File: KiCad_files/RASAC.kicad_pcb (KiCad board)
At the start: 6 copper layers, 147 x 85 mm, 386 parts, among them J1 PCIe_x4_Connector, J10 AS4C128M16D2A, J11 AS4C128M16D2A, J12 Conn_01x03, J13 Conn_02x03_Counter_Clockwise, J14 Conn_01x02, J2 PCIe_6_Pin_Power, J3 Conn_01x06, J4 USB_C_Receptacle, J5 TFP410, J6 DB15_Female_HighDensity_Mount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, J7 HDMI_A_1.4, J8 Conn_01x02, J9 Conn_01x02, Q1 Q_NMOS_GSD, Q2 Q_PMOS_GSD, SW1 SW_Push, U1 XC7A35T_CSG325, U10 W25Q128JV, U11 TPD12S521, U12 PCA9306, U13 LM2676-KTW, U2 MAX15027, U3 PI3420, U4 PI3421, U5 PI3420, U6 FT2232HL, U7 93LCxxC, U8 SiT8209, U9 SiT9102, Y1 12MHz

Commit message: PCB Layout
Don't remember what changed, but gonna push before my computer dies again
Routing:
- net VCC1V8: track 44.7 -> 146.7 mm, vias 0 -> 23
- net GND: vias 70 -> 115

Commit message: Initial FPGA routing + 3D RAM
Slowly losing insanity while listening to WII music for hours
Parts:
- J10, J11: footprint Housings_BGA:BGA-90_2x3x15_8.0x13.0mm_Pitch0.8mm -> custom:BGA-90_2x3x15_8.0x13.0mm_Pitch0.8mm
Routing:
- net VCC1V8: track 146.7 -> 213.3 mm, vias 23 -> 35
- net MGTAVCC: track 97.8 -> 125.2 mm, vias 2 -> 3
- net PCIe_RX2_P: track 29.4 -> 3.03 mm, vias 2 -> 1
- net PCIe_RX2_N: track 28.7 -> 2.92 mm, vias 2 -> 1
- net PCIe_RX1_P: track 26.7 -> 1.25 mm, vias 2 -> 0
- net GND: track 850.9 -> 875.9 mm, vias 115 -> 139
- net PCIe_RX3_N: track 28.1 -> 3.16 mm, vias 2 -> 1
- net PCIe_RX1_N: track 26.1 -> 1.19 mm, vias 2 -> 0
- net PCIe_RX3_P: track 28.8 -> 4.08 mm, vias 2 -> 1
- net PCIe_TX3_N: track 25.8 -> 1.27 mm, vias 2 -> 0
- net PCIe_TX3_P: track 26.4 -> 2.17 mm, vias 2 -> 0
- net PCIe_TX2_N: track 20.9 -> 1.26 mm, vias 2 -> 0
- net PCIe_TX2_P: track 21.5 -> 2.22 mm, vias 2 -> 0
- net PCIe_RX0_N: track 22.5 -> 3.16 mm, vias 2 -> 1
- net PCIe_RX0_P: track 23.1 -> 4.08 mm, vias 2 -> 1
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
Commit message: PCIe + RAM Layout?
Is this PCIe even going to work...?
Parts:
- U1: moved to B.Cu
- moved J13 29.0 mm to (105.6, 118.2)
- moved U10 17.3 mm to (116.3, 127.9)
- moved R1 9.12 mm to (117.5, 113.3)
- moved U8 9.12 mm to (113.8, 109.7)
- moved J14 9.12 mm to (116.2, 101.2)
- moved J9 9.12 mm to (123.1, 101.1)
- moved SW1 9.12 mm to (125.5, 110.5)
- moved U12 6.56 mm to (135.7, 106.6)
- moved J11 6.29 mm to (168.9, 114.3), turned to 270 degrees
- moved J10 5.24 mm to (168.9, 125.9), turned to 270 degrees
- moved U1 4.31 mm to (149.1, 126.3)
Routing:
- net VCC1V8: track 213.3 -> 93.9 mm, vias 35 -> 57
- net DDR2_DQSU_C: track 2.35 -> 46.3 mm, vias 0 -> 3
- net DDR2_DQSU_T: track 4.96 -> 36.7 mm, vias 1 -> 3
- net DDR2_DMU: track 2.36 -> 32.2 mm, vias 0 -> 1
- net PCIe_RX1_P: track 1.25 -> 29.0 mm, vias 0 -> 1
- net PCIe_RX1_N: track 1.19 -> 28.5 mm, vias 0 -> 1
- net DDR2_DQSL_T: track 4.16 -> 29.7 mm, vias 1 -> 3
- net DDR2_DQSL_C: track 4.97 -> 29.6 mm, vias 1 -> 4
- net DDR2_DML: track 1.41 -> 24.8 mm, vias 0 -> 3
- net PCIe_RX2_N: track 2.92 -> 26.0 mm, vias 1 -> 2
- net PCIe_RX2_P: track 3.03 -> 25.9 mm, vias 1 -> 2
- net PCIe_RX0_P: track 4.08 -> 25.6 mm
- net PCIe_RX0_N: track 3.16 -> 24.7 mm
- net DDR2_CK_T: track 1.40 -> 20.7 mm, vias 0 -> 2
- net DDR2_CK_C: track 4.93 -> 23.7 mm, vias 1 -> 3
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
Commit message: RAM+FPGA Attempt #1
Oh geez
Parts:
- J10: moved to B.Cu
- moved J10 45.2 mm to (124.2, 132.4)
- moved Q2 31.5 mm to (99.9, 150.9)
- moved Q1 31.5 mm to (101.4, 155.1)
- moved U10 23.5 mm to (100.4, 145.3)
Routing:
- net DDR2_DQ4: track 14.3 -> 40.8 mm, vias 1 -> 2
- net DDR2_DQ9: track 19.3 -> 41.2 mm, vias 2 -> 3
- net DDR2_DQ10: track 19.2 -> 38.8 mm, vias 3 -> 5
- net DDR2_DQ14: track 16.5 -> 35.0 mm, vias 1 -> 2
- net DDR2_DQ8: track 18.1 -> 36.3 mm, vias 1 -> 2
- net DDR2_DQ15: track 21.2 -> 39.1 mm, vias 2 -> 4
- net DDR2_DQ2: track 19.2 -> 36.8 mm, vias 3 -> 4
- net DDR2_DQ5: track 13.7 -> 30.9 mm
- net DDR2_A6: track 14.1 -> 29.1 mm, vias 1 -> 2
- net DDR2_DQ1: track 18.0 -> 32.7 mm, vias 2 -> 3
- net DDR2_A13: track 11.2 -> 25.7 mm
- net DDR2_A11: track 11.9 -> 25.6 mm, vias 1 -> 2
- net DDR2_A8: track 12.9 -> 26.3 mm
- net DDR2_DQ12: track 18.3 -> 31.2 mm, vias 2 -> 3
- net DDR2_DQ11: track 19.9 -> 32.8 mm, vias 3 -> 4
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
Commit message: RAM+FPGA Attempt #2
Plus some power connections
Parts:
- J11: moved to B.Cu
- moved J11 10.7 mm to (169.7, 124.9)
- moved J10 2.94 mm to (126.8, 131.2)
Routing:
- net GND: track 866.5 -> 944.3 mm, vias 171 -> 180
- net VCC1V8: track 93.9 -> 163.4 mm, vias 57 -> 59
- net DDR2_DQ6: track 13.2 -> 38.4 mm, vias 1 -> 2
- net DDR2_DQ3: track 17.1 -> 40.7 mm, vias 3 -> 4
- net DDR2_DQ0: track 18.2 -> 35.8 mm
- net DDR2_DQ7: track 15.4 -> 31.8 mm
- net DDR2_DQSU_T: track 36.7 -> 22.3 mm, vias 3 -> 2
- net DDR2_DQSU_C: track 34.9 -> 21.2 mm, vias 3 -> 2
- net DDR2_DMU: track 32.2 -> 19.2 mm
- net DDR2_DQ13: track 16.4 -> 28.9 mm, vias 1 -> 2
- net DDR2_DQSL_T: track 29.7 -> 18.5 mm, vias 3 -> 2
- net DDR2_DQ1: track 32.7 -> 43.5 mm
- net DDR2_DQSL_C: track 29.6 -> 19.3 mm, vias 4 -> 3
- net DDR2_DML: track 24.8 -> 15.0 mm, vias 3 -> 2
- net DDR2_DQ10: track 38.8 -> 29.1 mm, vias 5 -> 3
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- added copper zone on Power, net VCC1V8

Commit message: OH MY GOD
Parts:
- R1: moved to B.Cu
- moved C11 178.0 mm to (222.0, 121.6)
- moved TP6 157.3 mm to (220.6, 93.1)
- moved R5 73.6 mm to (114.6, 136.0), turned to 90 degrees
- moved TP16 64.9 mm to (112.4, 134.4)
- moved TP15 64.2 mm to (114.3, 133.4)
- moved R1 45.5 mm to (160.0, 129.7)
- moved J11 43.2 mm to (126.8, 119.6)
- moved Q1 29.1 mm to (117.1, 130.6), turned to 180 degrees
- moved Q2 22.2 mm to (117.1, 136.7)
- moved C211 21.3 mm to (65.9, 106.4)
- moved SW1 19.5 mm to (121.3, 91.5)
- moved U8 10.5 mm to (106.6, 102.1)
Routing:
- net PCIe_12V: track 226.6 -> 299.8 mm, vias 5 -> 46
- net PCIe_3.3V: track 0.00 -> 51.9 mm, vias 0 -> 4
- net PCIe_CLK_P: track 5.55 -> 34.0 mm, vias 1 -> 3
- net PCIe_CLK_N: track 5.15 -> 33.5 mm, vias 1 -> 3
- net MGTAVTT: track 65.1 -> 92.9 mm, vias 1 -> 3
- net DDR2_A0: track 24.4 -> 44.2 mm, vias 1 -> 2
- net DDR2_DQ24: track 15.9 -> 35.6 mm
- net DDR2_DQSU_T: track 22.3 -> 4.96 mm, vias 2 -> 1
- net DDR2_CK_T: track 12.6 -> 27.9 mm, vias 1 -> 2
- net DDR2_DQSU_C: track 21.2 -> 6.20 mm, vias 2 -> 0
- net GND: track 944.3 -> 929.5 mm, vias 180 -> 157
- net DDR2_DMU: track 19.2 -> 5.57 mm, vias 1 -> 0
- net DDR2_DQ31: track 14.8 -> 1.35 mm, vias 1 -> 0
- net DDR2_A2: track 20.4 -> 33.4 mm, vias 3 -> 4
- net DDR2_DQ30: track 14.3 -> 1.35 mm, vias 1 -> 0
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- added copper zone on Power, net PCIe_12V

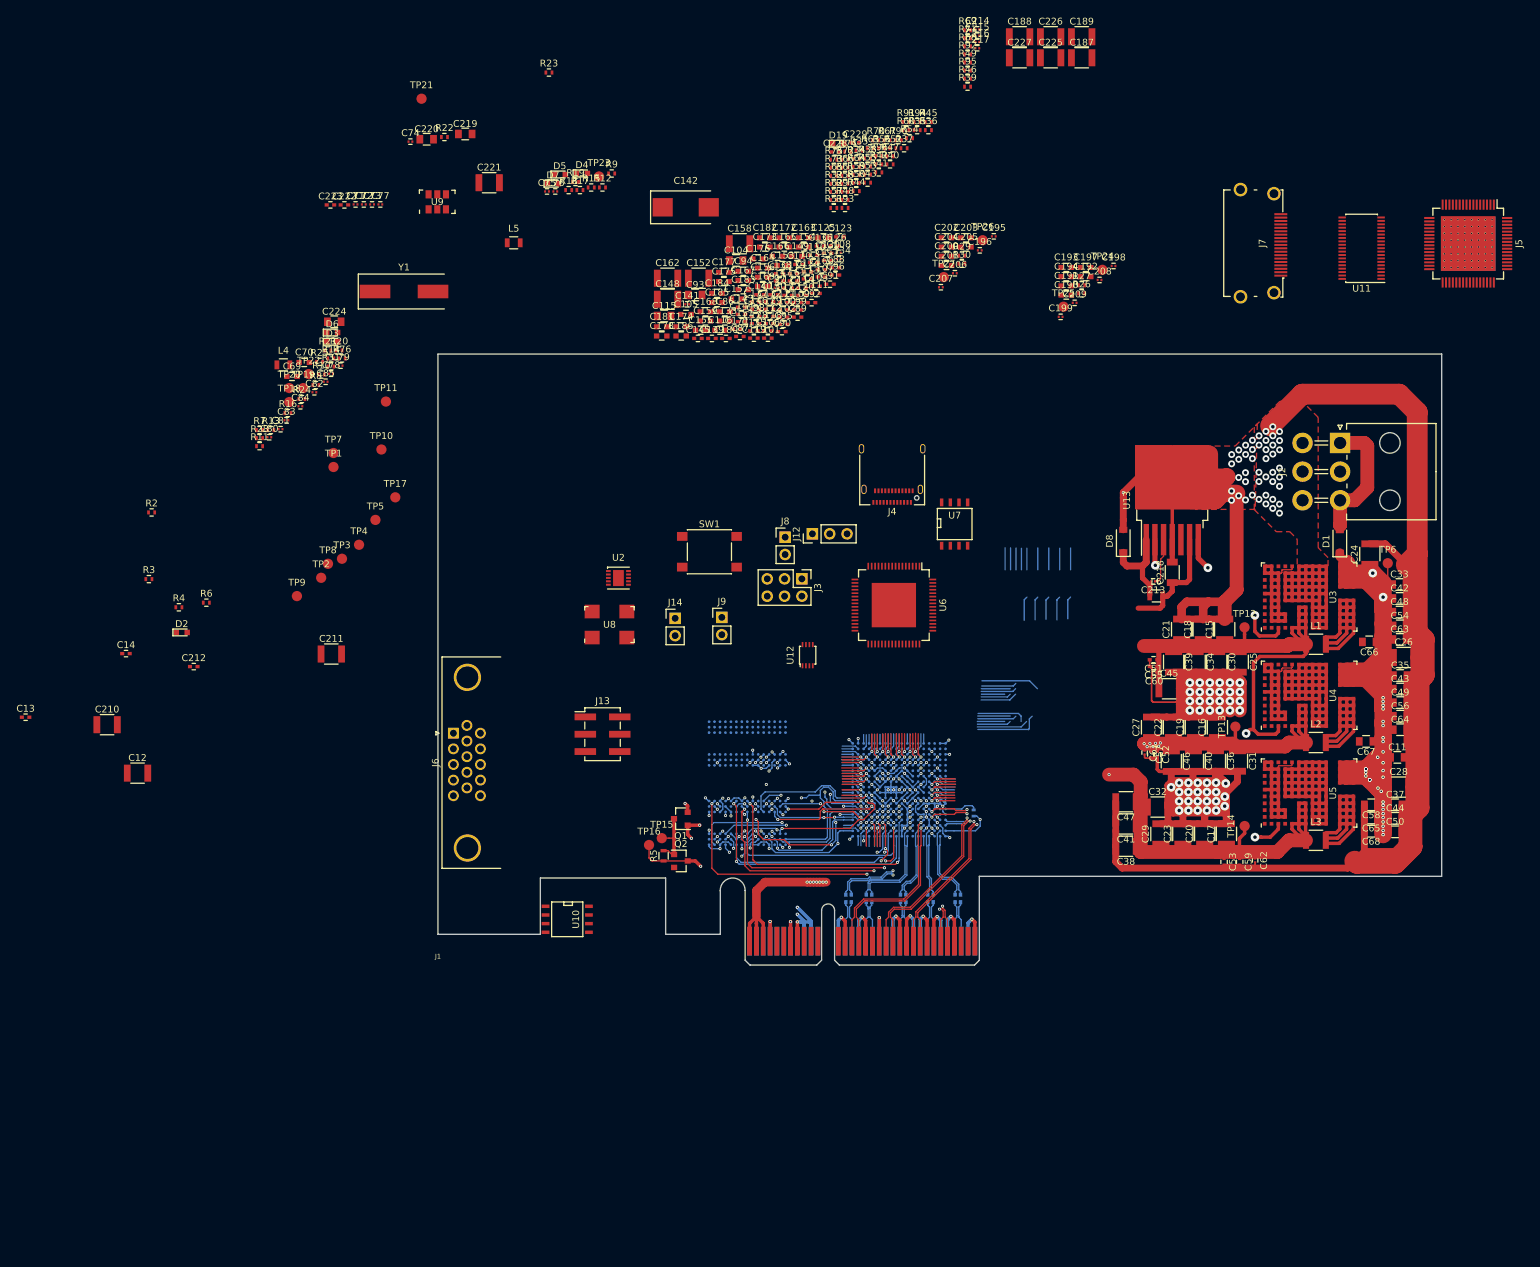
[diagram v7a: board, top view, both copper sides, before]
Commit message: Purged RAM (PCB) and updated RC footprints
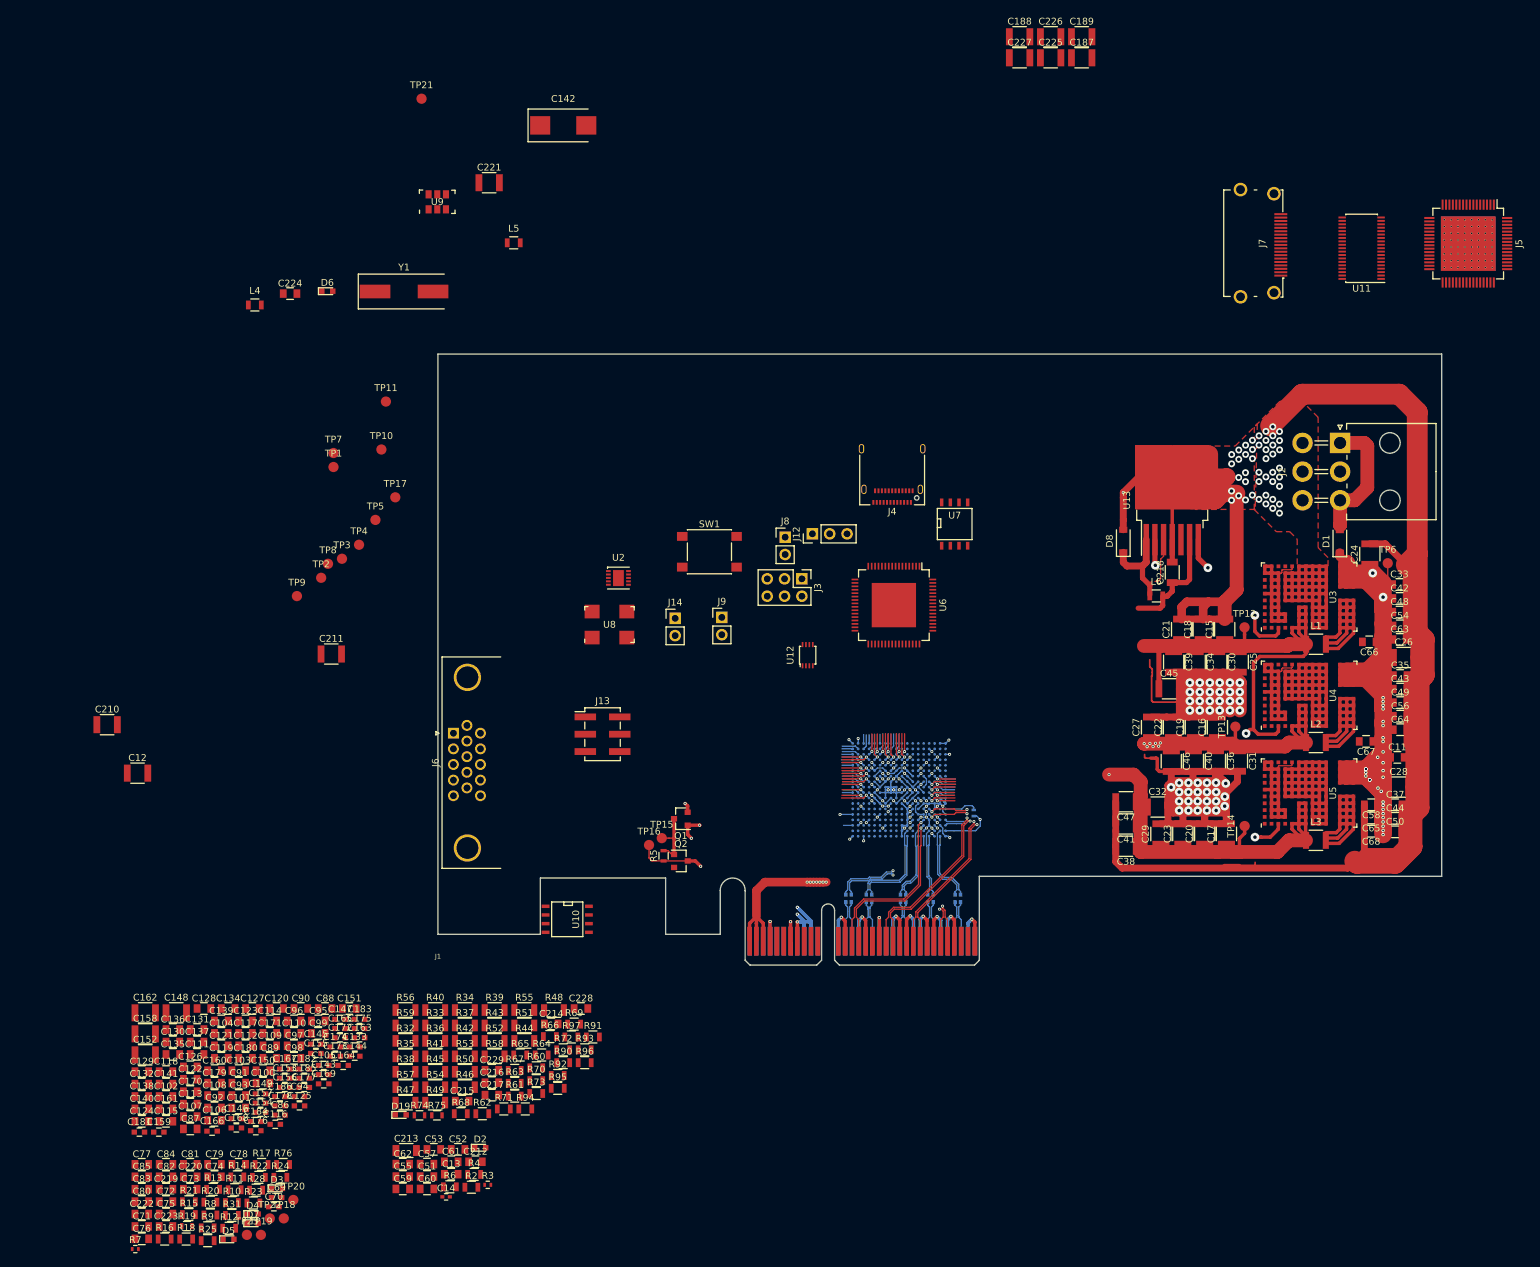
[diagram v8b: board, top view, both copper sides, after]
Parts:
- removed C190, C191, C192, C193, C194, C197, C200, C201, C202, C203, C204, C205: 4.7uF, Capacitors_SMD:C_0603
- removed C195, C196, C208, C209: 0.1uF, Capacitors_SMD:C_0201
- removed C198, C199, C206, C207: 0.068uF, Capacitors_SMD:C_0201
- removed J10, J11: AS4C128M16D2A, custom:BGA-90_2x3x15_8.0x13.0mm_Pitch0.8mm
- removed R26, R27, R29, R30: 4.7k, Resistors_SMD:R_0402
- removed TP24, TP25, TP26, TP27: TestPoint, Measurement_Points:Measurement_Point_Round-SMD-Pad_Small
- C100, C101, C102, C103, C106, C107, C109, C110, C111, C112, C113, C114, C117, C118, C119, C120, C121, C122, C123, C124, C126, C127, C128, C129, C13, C130, C131, C132, C135, C136, C137, C138, C139, C140, C150, C151, C160, C161, C170, C171, C179, C180, C212, C222, C223, C228, C229, C51, C52, C53, C55, C57, C59, C87, C88, C89, C90, C91, C92, C95, C96, C98, C99: footprint Capacitors_SMD:C_0402 -> Capacitors_SMD:C_0805
- C108, C134, C141, C214, C215, C216, C217, C60, C61, C62, C71, C72, C73, C74, C75, C76, C77, C78, C79, C80, C81, C82, C83, C84, C85, C97: footprint Capacitors_SMD:C_0201 -> Capacitors_SMD:C_0805
- C143, C144, C145, C146, C147: footprint Capacitors_SMD:C_0402 -> Capacitors_SMD:C_0603
- C213: footprint Capacitors_SMD:C_0201 -> Capacitors_SMD:C_1206
- R10, R11, R12, R13, R14, R15, R16, R17, R18, R2, R20, R21, R22, R23, R24, R25, R28, R31, R4, R6, R60, R61, R62, R63, R64, R65, R66, R67, R68, R69, R70, R71, R72, R73, R76, R8, R9, R90, R91, R92, R93, R94, R95, R96, R97: footprint Resistors_SMD:R_0402 -> Resistors_SMD:R_0805
- R19, R75: footprint Resistors_SMD:R_0402 -> Resistors_SMD:R_0603
- R32, R33, R34, R35, R36, R37, R38, R39, R40, R41, R42, R43, R44, R45, R46, R47, R48, R49, R50, R51, R52, R53, R54, R55, R56, R57, R58, R59: footprint Resistors_SMD:R_0402 -> Resistors_SMD:R_1206
- R74: footprint Resistors_SMD:R_0402_NoSilk -> Resistors_SMD:R_0603
- moved C215 173.4 mm to (85.0, 171.9)
- moved R68 173.1 mm to (84.8, 173.8)
- moved R23 171.2 mm to (54.5, 186.9)
- moved R49 171.2 mm to (81.1, 172.2)
- moved R71 170.9 mm to (91.1, 173.1)
- moved C217 169.0 mm to (89.4, 171.0)
- moved C216 168.2 mm to (89.4, 169.2)
- moved R9 165.4 mm to (47.8, 190.5)
- moved R46 165.1 mm to (85.4, 169.9)
- moved C76 165.0 mm to (38.1, 192.1)
- moved R18 163.6 mm to (44.6, 192.1)
- moved TP23 163.4 mm to (53.5, 191.5)
- moved D5 163.4 mm to (50.8, 192.2)
- moved R19 163.2 mm to (44.7, 190.2)
- moved R12 162.0 mm to (50.9, 190.6)
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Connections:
- R61 pad 2: Net-(R61-Pad2) -> VGA_R1
- U1 pad E18: DDR2_CK_T -> Net-(U1-PadE18)
- U1 pad F14: DDR2_DQSU_T -> Net-(U1-PadF14)
- U1 pad F15: DDR2_DQSL_T -> Net-(U1-PadF15)
- U1 pad F17: DDR2_DMU -> Net-(U1-PadF17)
- U1 pad G14: DDR2_DQSL_C -> Net-(U1-PadG14)
- U1 pad G15: DDR2_RAS_B -> Net-(U1-PadG15)
- U1 pad G16: DDR2_CAS_B -> Net-(U1-PadG16)
- U1 pad H14: DDR2_CK_C -> Net-(U1-PadH14)
- U1 pad H16: DDR2_WE_B -> Net-(U1-PadH16)
- U1 pad H17: DDR2_DQSU_C -> Net-(U1-PadH17)
- U1 pad H18: DDR2_DML -> Net-(U1-PadH18)
- U1 pad J4: DDR2_DQ4 -> Net-(U1-PadJ4)
- U1 pad J5: DDR2_DQ3 -> Net-(U1-PadJ5)
- U1 pad J6: DDR2_DQ0 -> Net-(U1-PadJ6)
- U1 pad K1: DDR2_DQ6 -> Net-(U1-PadK1)
- U1 pad K2: DDR2_DQ5 -> Net-(U1-PadK2)
- U1 pad K3: DDR2_DQ7 -> Net-(U1-PadK3)
- U1 pad K5: DDR2_DQ2 -> Net-(U1-PadK5)
- U1 pad K6: DDR2_DQ1 -> Net-(U1-PadK6)
- U1 pad L2: DDR2_DQ8 -> Net-(U1-PadL2)
- U1 pad L3: DDR2_DQ10 -> Net-(U1-PadL3)
- U1 pad L4: DDR2_DQ9 -> Net-(U1-PadL4)
- U1 pad L5: DDR2_DQ11 -> Net-(U1-PadL5)
- U1 pad M1: DDR2_DQ14 -> Net-(U1-PadM1)
- U1 pad M2: DDR2_DQ13 -> Net-(U1-PadM2)
- U1 pad M4: DDR2_DQ19 -> Net-(U1-PadM4)
- U1 pad M5: DDR2_DQ12 -> Net-(U1-PadM5)
- U1 pad M6: DDR2_DQ15 -> Net-(U1-PadM6)
- U1 pad N1: DDR2_DQ17 -> Net-(U1-PadN1)
- U1 pad N2: DDR2_DQ22 -> Net-(U1-PadN2)
- U1 pad N3: DDR2_DQ21 -> Net-(U1-PadN3)
- U1 pad N4: DDR2_DQ20 -> Net-(U1-PadN4)
- U1 pad N6: DDR2_DQ16 -> Net-(U1-PadN6)
- U1 pad P1: DDR2_DQ18 -> Net-(U1-PadP1)
- U1 pad P3: DDR2_DQ24 -> Net-(U1-PadP3)
- U1 pad P4: DDR2_DQ23 -> Net-(U1-PadP4)
- U1 pad P5: DDR2_A6 -> Net-(U1-PadP5)
- U1 pad P6: DDR2_A5 -> Net-(U1-PadP6)
- U1 pad R1: DDR2_DQ26 -> Net-(U1-PadR1)
- U1 pad R2: DDR2_DQ25 -> Net-(U1-PadR2)
- U1 pad R3: DDR2_DQ27 -> Net-(U1-PadR3)
- U1 pad R5: DDR2_A9 -> Net-(U1-PadR5)
- U1 pad R6: DDR2_CKE -> Net-(U1-PadR6)
- U1 pad R7: DDR2_A11 -> Net-(U1-PadR7)
- U1 pad T2: DDR2_DQ28 -> Net-(U1-PadT2)
- U1 pad T3: DDR2_A2 -> Net-(U1-PadT3)
- U1 pad T4: DDR2_A1 -> Net-(U1-PadT4)
- U1 pad T5: DDR2_A10 -> Net-(U1-PadT5)
- U1 pad T7: DDR2_A12 -> Net-(U1-PadT7)
- U1 pad U1: DDR2_DQ30 -> Net-(U1-PadU1)
- U1 pad U2: DDR2_DQ29 -> Net-(U1-PadU2)
- U1 pad U4: DDR2_A3 -> Net-(U1-PadU4)
- U1 pad U5: DDR2_A8 -> Net-(U1-PadU5)
- U1 pad U6: DDR2_A7 -> Net-(U1-PadU6)
- U1 pad U7: DDR2_A13 -> Net-(U1-PadU7)
- U1 pad V2: DDR2_A0 -> Net-(U1-PadV2)
- U1 pad V3: DDR2_DQ31 -> Net-(U1-PadV3)
- U1 pad V4: DDR2_A4 -> Net-(U1-PadV4)
- U1 pad V6: DDR2_BA0 -> Net-(U1-PadV6)
- U1 pad V7: DDR2_BA2 -> Net-(U1-PadV7)
- U1 pad V8: DDR2_BA1 -> Net-(U1-PadV8)
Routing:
- net DDR2_A0: track 44.2 -> 0.00 mm, vias 2 -> 0
- net DDR2_DQ14: track 40.8 -> 0.00 mm, vias 4 -> 0
- net DDR2_DQ1: track 40.5 -> 0.00 mm, vias 3 -> 0
- net DDR2_DQ3: track 40.2 -> 0.00 mm, vias 3 -> 0
- net DDR2_DQ4: track 37.0 -> 0.00 mm, vias 2 -> 0
- net DDR2_DQ6: track 36.3 -> 0.00 mm, vias 2 -> 0
- net DDR2_DQ24: track 35.6 -> 0.00 mm, vias 2 -> 0
- net DDR2_DQ11: track 34.7 -> 0.00 mm, vias 5 -> 0
- net DDR2_A4: track 34.5 -> 0.00 mm, vias 2 -> 0
- net DDR2_A2: track 33.4 -> 0.00 mm, vias 4 -> 0
- net DDR2_DQ0: track 32.7 -> 0.00 mm, vias 2 -> 0
- net DDR2_DQ9: track 32.6 -> 0.00 mm, vias 2 -> 0
- net DDR2_DQ7: track 30.9 -> 0.00 mm, vias 2 -> 0
- net DDR2_A11: track 30.8 -> 0.00 mm, vias 3 -> 0
- net DDR2_A8: track 30.5 -> 0.00 mm, vias 2 -> 0
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- removed copper zone on Power, net VCC1V8
